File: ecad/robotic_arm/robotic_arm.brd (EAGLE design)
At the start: 61.1 x 57.9 mm, 125 parts, among them J1 5A/28V, SW1 5A/28V, Y1 16 MHz

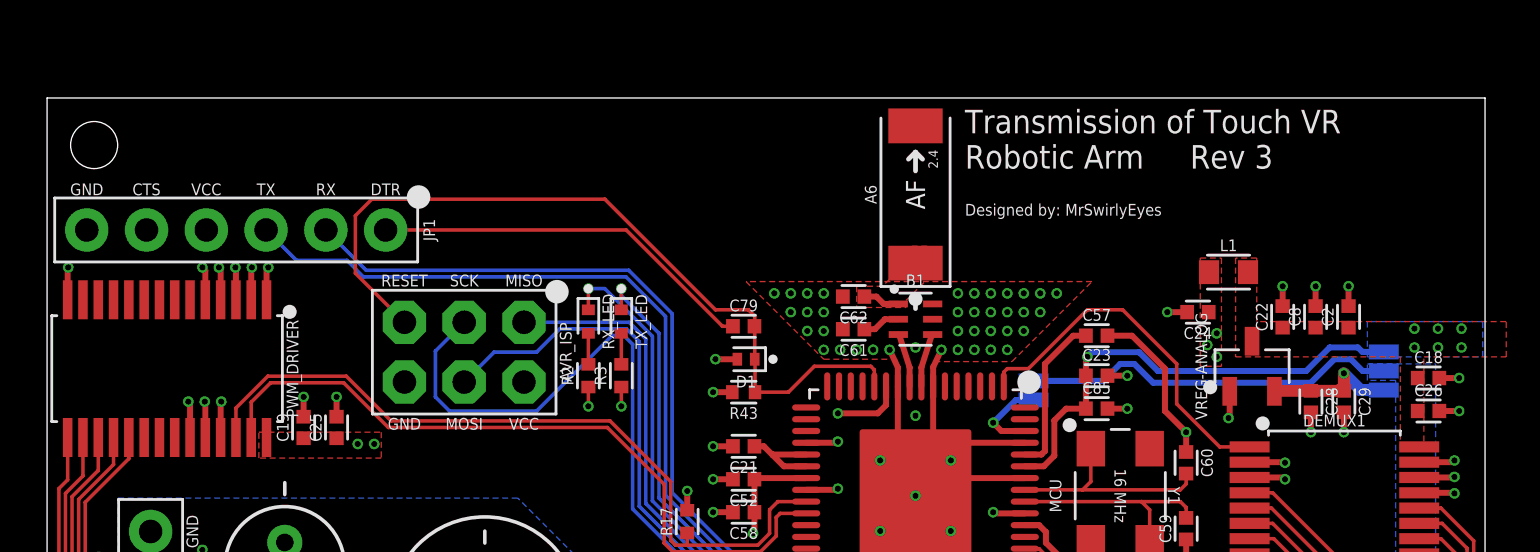
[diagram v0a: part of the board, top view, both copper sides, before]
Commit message: Update Robotic Arm to use new EAGLE library names.
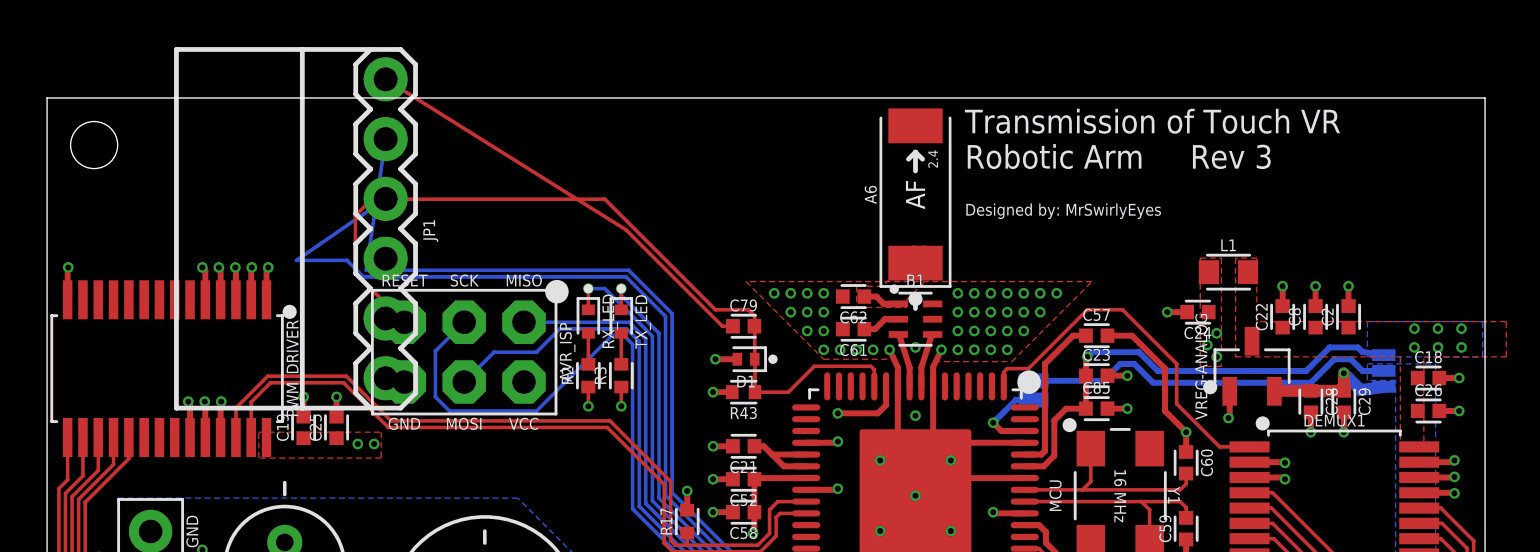
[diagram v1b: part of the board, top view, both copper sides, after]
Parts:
- A6: device PiB_radio_frequency:ANTC6522X100 -> _radio_frequency:ANTC6522X100
- AVR_ISP: device PiB_connectors:HDRV6W64P254_2X3_762X483X838B_AVR-ISP -> _connectors:HDRV6W64P254_2X3_762X483X838B_AVR-ISP
- B1: device PiB_radio_frequency:RESCAXE65P200X125X95-6 -> _radio_frequency:RESCAXE65P200X125X95-6
- C1, C10, C12, C14, C16, C18, C19, C2, C21, C22, C23, C24, C25, C26, C28, C29, C3, C30, C4, C47, C48, C49, C5, C50, C51, C52, C54, C55, C57, C58, C59, C6, C60, C61, C62, C63, C7, C79, C8, C83, C85, C92, C93, C96, C98: device PiB_capacitors:CAPC1005X55_SMD-0402 -> _capacitors:CAPC1005X55_SMD-0402
- C11, C13, C15, C17, C9: device PiB_capacitors:_AE_PTH-DIA5-LS2-H11 -> _capacitors:_AE_PTH-DIA5-LS2-H11
- C20, C27, C80: device PiB_capacitors:_AE_PTH_DIA8-LS3.5-H21.50 -> _capacitors:_AE_PTH_DIA8-LS3.5-H21.50
- C53: value 1uF/25V -> 0.1uF/50V; device PiB_capacitors:CAPC1005X55_SMD-0402 -> _capacitors:CAPC1005X55_SMD-0402
- C94, C95, C97: device PiB_capacitors:CAPC2012X95_SMD-0805 -> _capacitors:CAPC2012X95_SMD-0805
- D1: device PiB_discrete_semiconductors:DFN100X60X55-2 -> _discrete_semiconductors:DFN100X60X55-2
- D2, D7: device PiB_discrete_semiconductors:SODFL3516X170 -> _discrete_semiconductors:SODFL3516X170
- DEMUX1: device PiB:SOP65P780X200-24 -> _special:SOP65P780X200-24
- FSR_INDEX, FSR_MIDDLE, FSR_PALM, FSR_PINKY, FSR_RING, FSR_THUMB: device PiB_sensors:_MOLEX-0530470210_VERT_PITCH-1.25MM -> _sensors:_MOLEX-0530470210_VERT_PITCH-1.25MM
- J1: device PiB_connectors:POWER_JACK_PTH_ID2.1MM-OD5.5MM -> _connectors:POWER_JACK_PTH_ID2.1MM-OD5.5MM
- JP1: device PiB_connectors:HDRV6W64P254_1X6_1524X254X838B_FTDI -> _connectors:FTDI_BASIC-6PIN-MALE-RA
- JP2: device PiB_connectors:SMT-JUMPER_2_NO_SILK -> _connectors:SMT-JUMPER_2_NO_SILK
- JP3: value JUMPER_SMD_3-PAD_NO_NO-SILK -> JUMPER_SMD_3-PAD_NO_SILK; device PiB_connectors:SMT-JUMPER_3_NO_NO-SILK -> _connectors:SMT-JUMPER_3_NO_SILK
- L1, L2: device PiB_inductors:INDC1608X60-0603 -> _inductors:INDC1608X60-0603
- LED1, RX_LED, TX_LED: device PiB_leds:LEDC1005X40_LED-0402 -> _leds:LEDC1005X40_LED-0402
- LIPO1: device PiB_batteries:1X02_WIRE_CONNECTOR_AWG-18 -> _batteries:1X02_WIRE_CONNECTOR_AWG-18
- MCU: device PiB_ic_microcontrollers:QFN50P900X900X90-64 -> _ic_microcontrollers:QFN50P900X900X90-64
- NOISE_BR, NOISE_BR1: device PiB_power_symbols:NET_BRIDGE -> _power_symbols:NET_BRIDGE
- PWM_DRIVER: device PiB:SOP65P650X110-28 -> _special:SOP65P650X110-28
- R1, R10, R12, R13, R14, R15, R16, R17, R18, R2, R3, R39, R4, R40, R41, R42, R43, R5, R6, R7, R8, R9: device PiB_resistors:RESC1005X35_SMD-0402 -> _resistors:RESC1005X35_SMD-0402
- SERVO_INDEX, SERVO_MIDDLE, SERVO_PINKY, SERVO_RING, SERVO_THUMB: device PiB_motors:HDRV3W64P254_1X3_762X254X838B -> _motors:HDRV3W64P254_1X3_762X254X838B
- SW1: device PiB_switches:SW_TOGGLE_SPDT_5A-28V_13L-7W -> _switches:SW_TOGGLE_SPDT_5A-28V_13L-7W
- TEMP_INDEX, TEMP_MIDDLE, TEMP_PINKY, TEMP_RING, TEMP_THUMB: device PiB_sensors:_MOLEX-0530470310_VERT_PITCH-1.25MM -> _sensors:_MOLEX-0530470310_VERT_PITCH-1.25MM
- VREG-ANALOG: device PiB_ic_power:SOT95P237X112-3_SOT-23-3 -> _ic_power:SOT95P237X112-3_SOT-23-3
- VREG-MCU: device PiB_ic_power:SOIC127P600X265-8 -> _ic_power:SOIC127P600X265-8
- VREG-SERVOS: device PiB_ic_power:TO170P1363X457-6 -> _ic_power:TO170P1363X457-6
- Y1: device PiB_crystals_oscillators_resonators:OSCCC500X320X110_CRYSTAL -> _crystals_oscillators_resonators:OSCCC500X320X110_CRYSTAL
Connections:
- net RX: now also JP1.TXO; no longer JP1.TX
- net TX: now also JP1.RXI; no longer JP1.RX
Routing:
- net TX: track 42.1 -> 45.3 mm
- net RX: track 43.8 -> 46.6 mm
- net N$41: track 16.5 -> 18.3 mm

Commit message: Remove components that I believe are unecessary or redundant.
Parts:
- removed C18, C25: 10uF/6.3V, _capacitors:CAPC1005X55_SMD-0402
- removed R12, R14, R4, R6, R8: 10K, _resistors:RESC1005X35_SMD-0402
- removed R13, R15, R5, R7, R9: 100, _resistors:RESC1005X35_SMD-0402
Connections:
- removed net N$4: R9.1, SERVO_THUMB.SIG
- removed net N$6: R7.1, SERVO_INDEX.SIG
- removed net N$7: R5.1, SERVO_MIDDLE.SIG
- removed net N$8: R15.1, SERVO_RING.SIG
- removed net N$9: R13.1, SERVO_PINKY.SIG
- net 3.3V: no longer C25.1
- net A3.3V: no longer C18.1
- net AGND: no longer C18.2
- net GND: no longer C25.2, R12.1, R14.1, R4.1, R6.1, R8.1
- net SERVO_INDEX: now also SERVO_INDEX.SIG; no longer R6.2, R7.2
- net SERVO_MIDDLE: now also SERVO_MIDDLE.SIG; no longer R4.2, R5.2
- net SERVO_PINKY: now also SERVO_PINKY.SIG; no longer R12.2, R13.2
- net SERVO_RING: now also SERVO_RING.SIG; no longer R14.2, R15.2
- net SERVO_THUMB: now also SERVO_THUMB.SIG; no longer R8.2, R9.2
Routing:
- net GND: track 53.2 -> 48.3 mm, vias 40 -> 34
- net N$9: track 2.21 -> 0.00 mm
- net N$8: track 2.21 -> 0.00 mm
- net N$7: track 2.21 -> 0.00 mm
- net N$6: track 2.21 -> 0.00 mm
- net N$4: track 2.21 -> 0.00 mm
- net SERVO_MIDDLE: track 25.7 -> 24.0 mm
- net SERVO_INDEX: track 17.5 -> 15.9 mm
- net SERVO_THUMB: track 9.34 -> 7.72 mm
- net SERVO_RING: track 33.8 -> 32.2 mm
- net SERVO_PINKY: track 42.0 -> 40.4 mm
- net AGND: track 51.2 -> 50.3 mm, vias 77 -> 76

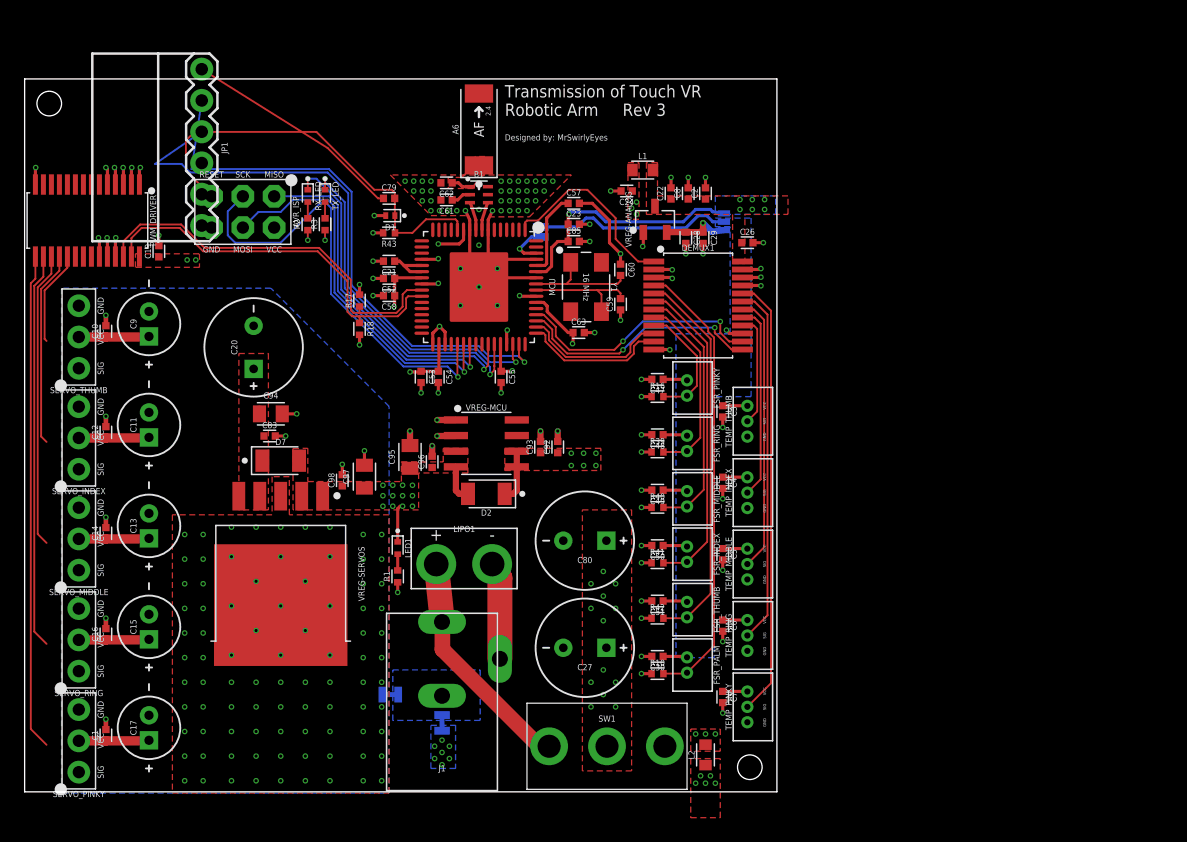
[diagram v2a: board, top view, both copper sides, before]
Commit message: Create mcu to unity example code.  Create schematics for master thesis.  Edit robotic arm and touch glove pcb.
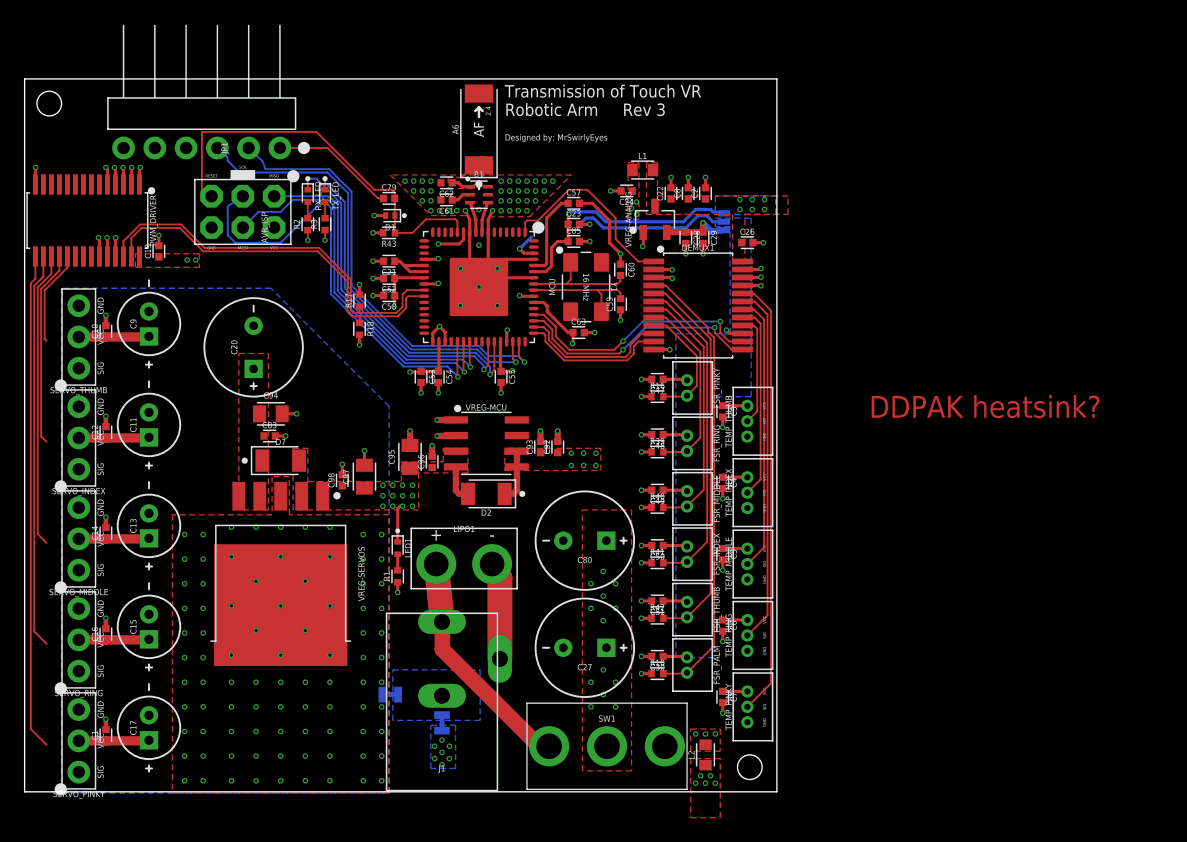
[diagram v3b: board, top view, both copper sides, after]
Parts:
- removed JP2: JUMPER_SMD_2-PAD_NO_SILK, _connectors:SMT-JUMPER_2_NO_SILK
- AVR_ISP: value PTH VERT MALE -> AVR ISP; device _connectors:HDRV6W64P254_2X3_762X483X838B_AVR-ISP -> _connectors:HDRV6W64P254_2X3_762X508X838B
- JP1: value FTDI -> PTH RA VERT MALE; device _connectors:FTDI_BASIC-6PIN-MALE-RA -> _connectors:HDRRA6W64P254_1X6_1524X254X254B_FTDI
- moved AVR_ISP 2.84 mm to (17.7, 47.2)
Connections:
- removed net AREF: JP2.2, MCU.62
- net A1.8V: now also MCU.62
- net VSENSOR: no longer JP2.1
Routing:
- net TX: track 45.3 -> 36.1 mm
- net RX: track 46.6 -> 37.8 mm
- net N$41: track 18.3 -> 10.1 mm
- net AREF: track 3.61 -> 0.00 mm, vias 1 -> 0
- net VSENSOR: track 28.0 -> 25.0 mm
- net A1.8V: track 5.73 -> 8.39 mm, vias 1 -> 2
- net GND: track 48.3 -> 47.0 mm
- net 3.3V: track 25.1 -> 25.9 mm
- net RESET: track 34.3 -> 33.6 mm
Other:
- board text added: "DDPAK heatsink?"

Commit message: Create PCA9685Servo library.  Update robotic arm PCB to Rev 3.  Ready for fab.
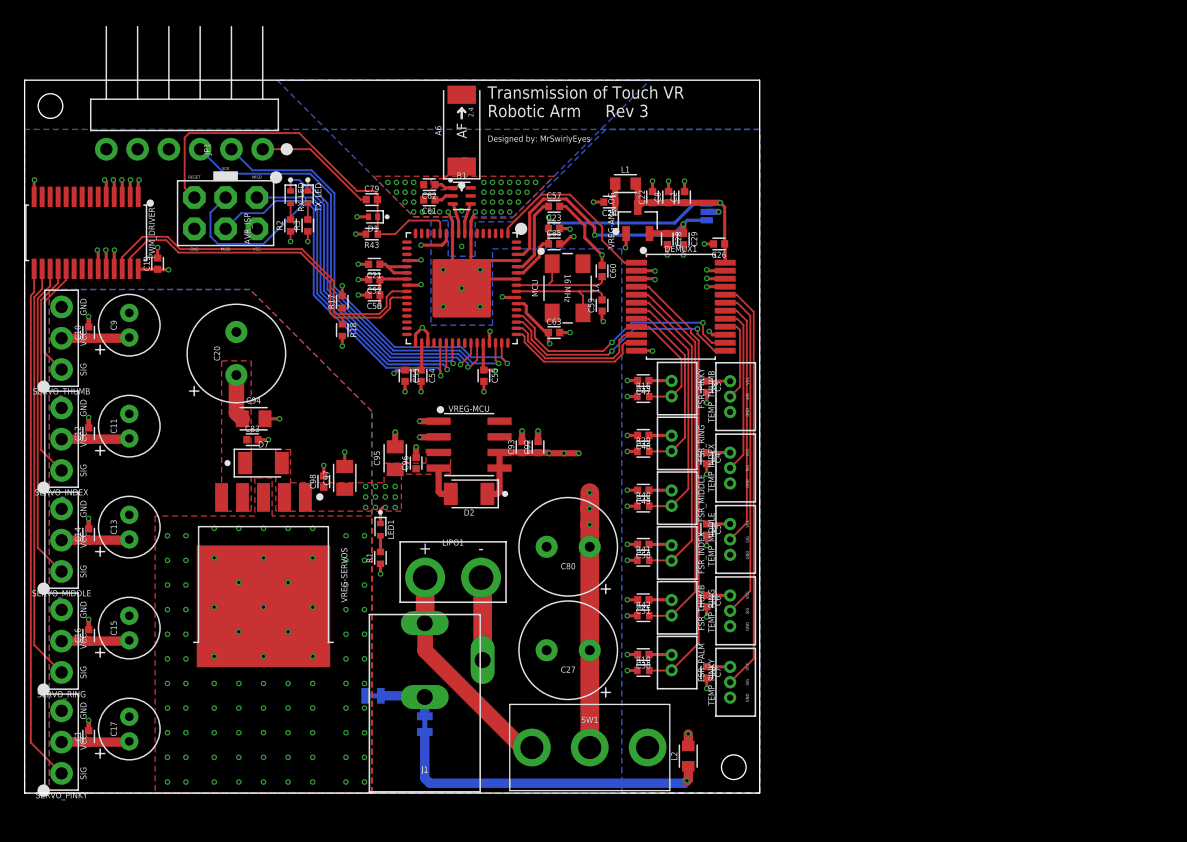
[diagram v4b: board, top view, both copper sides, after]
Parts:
- C11, C13, C15, C17, C9: device _capacitors:_AE_PTH-DIA5-LS2-H11 -> _capacitors:CAPPRD200W50D500H1100B
- C20, C27, C80: device _capacitors:_AE_PTH_DIA8-LS3.5-H21.50 -> _capacitors:CAPPRD350W60D800H2000B
- moved TEMP_THUMB 2.44 mm to (57.3, 32.2)
- moved TEMP_INDEX 2.44 mm to (57.3, 26.4)
- moved TEMP_MIDDLE 2.44 mm to (57.3, 20.6)
- moved TEMP_PINKY 2.44 mm to (57.3, 9.00)
- moved TEMP_RING 2.44 mm to (57.3, 14.8)
- moved C7 2.39 mm to (55.4, 9.80)
- moved C3 2.39 mm to (55.4, 33.0)
- moved C4 2.39 mm to (55.4, 27.2)
- moved C5 2.39 mm to (55.4, 21.4)
- moved C6 2.39 mm to (55.4, 15.6)
- moved C26 2.30 mm to (56.4, 44.6), turned to 180 degrees
- moved LED1 2.05 mm to (28.9, 21.4)
- moved R1 2.05 mm to (28.9, 19.1)
- moved C63 2.00 mm to (43.0, 37.4)
- moved L1 1.78 mm to (48.8, 49.5)
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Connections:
- net 5V: now also C11.A, C13.A, C15.A, C17.A, C20.A, C9.A; no longer C11.+, C13.+, C15.+, C17.+, C20.+, C9.+
- net GND: now also C27.K, C80.K; no longer C27.-, C80.-
- net NGND: now also C11.K, C13.K, C15.K, C17.K, C20.K, C9.K; no longer C11.-, C13.-, C15.-, C17.-, C20.-, C9.-
- net VBAT: now also C27.A, C80.A; no longer C27.+, C80.+
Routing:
- net A3.3V: track 30.4 -> 94.9 mm, vias 7 -> 2
- net VSENSOR: track 25.0 -> 66.9 mm, vias 0 -> 1
- net N$1: track 0.00 -> 26.5 mm, vias 12 -> 1
- net VBAT: track 6.36 -> 25.3 mm, vias 25 -> 15
- net A1.8V: track 8.39 -> 24.6 mm
- net 3.3V: track 25.9 -> 35.9 mm, vias 19 -> 13
- net GND: track 47.0 -> 51.7 mm
- net 5V: track 28.8 -> 31.4 mm
- net TEMP_INDEX: track 15.9 -> 13.8 mm
- net TEMP_PINKY: track 35.9 -> 33.8 mm
- net TEMP_MIDDLE: track 22.5 -> 20.4 mm
- net TEMP_THUMB: track 9.14 -> 7.04 mm
- net TEMP_RING: track 29.2 -> 27.1 mm
- net SDA: track 31.7 -> 29.7 mm
- net SCL: track 32.5 -> 30.6 mm
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- added copper zone on layer 16, net AGND
- removed copper zone on layer 1, net 3.3V
- removed copper zone on layer 1, net A3.3V
- removed copper zone on layer 15, net A3.3V
- removed copper zone on layer 16, net A3.3V
- removed copper zone on layer 1, net N$1
- removed copper zone on layer 16, net N$1
- removed copper zone on layer 2, net N$1
- removed copper zone on layer 16, net VSENSOR
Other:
- board size 61.1 x 57.9 mm -> 59.7 x 57.9 mm
- board text removed: "DDPAK heatsink?"

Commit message: Moved some text on the robotic arm board.
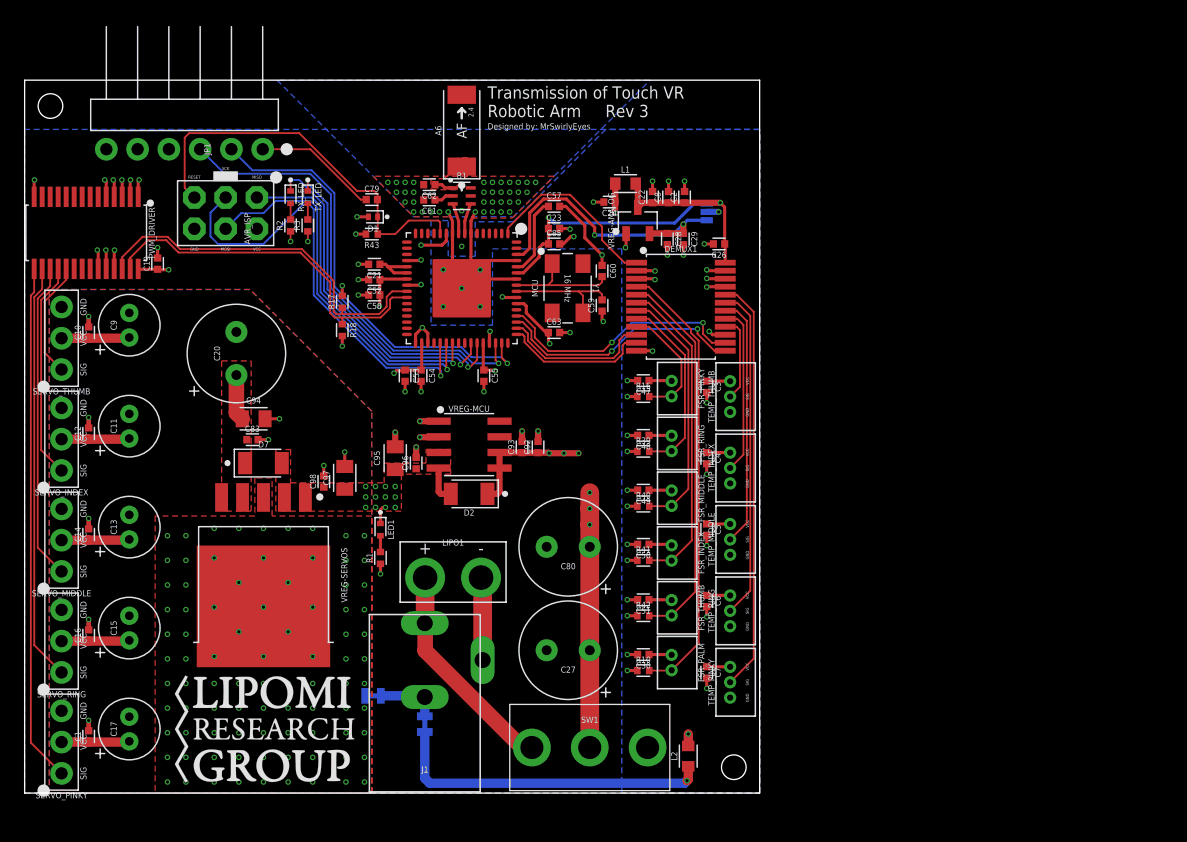
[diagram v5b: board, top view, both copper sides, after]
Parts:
- flipped U$21 to the top
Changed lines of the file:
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@@
 <setting verticaltext="up"/>
 </settings>
-<grid distance="1" unitdist="mm" unit="mm" style="lines" multiple="1" display="yes" altdistance="0.1" altunitdist="mm" altunit="mm"/>
+<grid distance="1" unitdist="mm" unit="mm" style="lines" multiple="1" display="no" altdistance="0.1" altunitdist="mm" altunit="mm"/>
 <layers>
 <layer number="1" name="Top" color="4" fill="1" visible="yes" active="yes"/>
@@
 <layer number="25" name="tNames" color="7" fill="1" visible="yes" active="yes"/>
 <layer number="26" name="bNames" color="7" fill="1" visible="yes" active="yes"/>
-<layer number="27" name="tValues" color="7" fill="1" visible="no" active="yes"/>
+<layer number="27" name="tValues" color="7" fill="1" visible="yes" active="yes"/>
 <layer number="28" name="bValues" color="7" fill="1" visible="yes" active="yes"/>
 <layer number="29" name="tStop" color="7" fill="3" visible="yes" active="yes"/>
@@
 <text x="37.6" y="54.9" size="1" layer="21" font="vector" ratio="20">Transmission of Touch VR
 Robotic Arm     Rev 3</text>
-<text x="37.6" y="52.9" size="0.5" layer="21" font="vector" ratio="10">Designed by: MrSwirlyEyes</text>
+<text x="37.6" y="53.9" size="0.5" layer="21" font="vector" ratio="10">Designed by: MrSwirlyEyes</text>
 <text x="37.6" y="55.9" size="1" layer="22" font="vector" ratio="20" rot="MR180">Transmission of Touch VR
 Robotic Arm     Rev 3</text>
@@
 </element>
 <element name="U$20" library="PiB_logo" package="MRSWIRLYEYES-LOGO" value="" x="24.6" y="32.9" smashed="yes" rot="MR0"/>
-<element name="U$21" library="PiB_logo" package="LRG-LOGO" value="" x="19.5" y="5.2" smashed="yes" rot="MR0"/>
+<element name="U$21" library="PiB_logo" package="LRG-LOGO" value="" x="19.5" y="5.2" smashed="yes"/>
 <element name="D2" library="_discrete_semiconductors" package="SODFL3516X170" package3d_urn="urn:adsk.eagle:package:2939213/1" value="1A/50V" x="36.1" y="24.3" smashed="yes" rot="R180">
 <attribute name="DATASHEET" value="http://www.comchiptech.com/cms/UserFiles/CGRKM4001-HF%20Thru.%20CGRKM4007-HF%20RevG.pdf" x="36.1" y="24.3" size="1.778" layer="27" rot="R180" display="off"/>
